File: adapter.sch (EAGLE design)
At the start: 14 parts

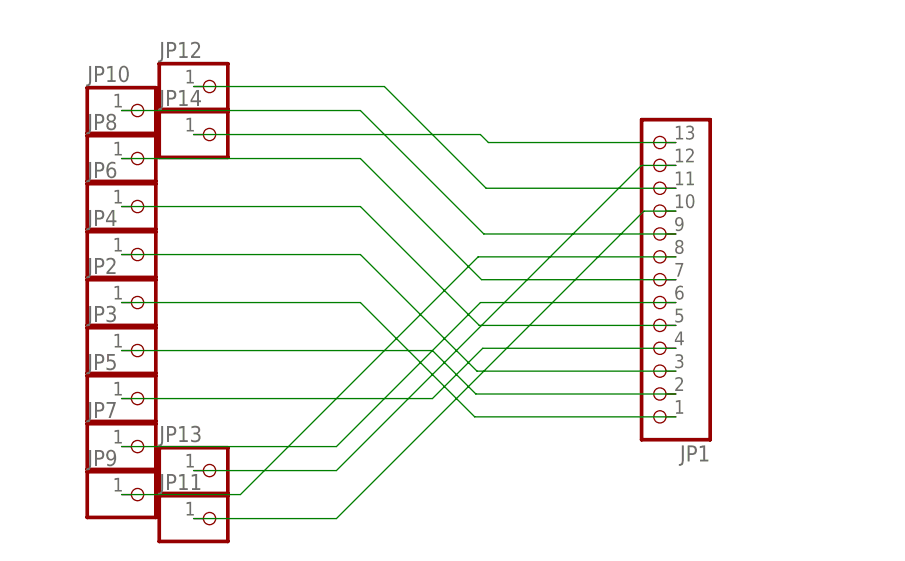
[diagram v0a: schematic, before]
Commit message: update adapter board for SMD
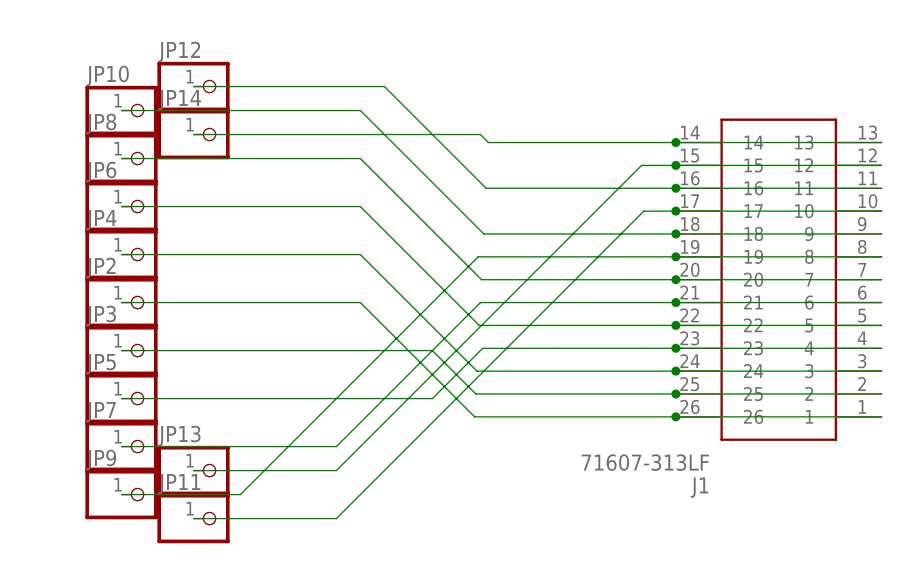
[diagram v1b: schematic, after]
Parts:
- removed JP1: (no value), pinhead:PINHD-1X13
- added J1: 71607-313LF, ltobms:71607-313LF
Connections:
- net N$1: now also J1.1, J1.26; no longer JP1.1
- net N$10: now also J1.10, J1.17; no longer JP1.10
- net N$11: now also J1.11, J1.16; no longer JP1.11
- net N$12: now also J1.12, J1.15; no longer JP1.12
- net N$13: now also J1.13, J1.14; no longer JP1.13
- net N$2: now also J1.2, J1.25; no longer JP1.2
- net N$3: now also J1.24, J1.3; no longer JP1.3
- net N$4: now also J1.23, J1.4; no longer JP1.4
- net N$5: now also J1.22, J1.5; no longer JP1.5
- net N$6: now also J1.21, J1.6; no longer JP1.6
- net N$7: now also J1.20, J1.7; no longer JP1.7
- net N$8: now also J1.19, J1.8; no longer JP1.8
- net N$9: now also J1.18, J1.9; no longer JP1.9

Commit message: add labels
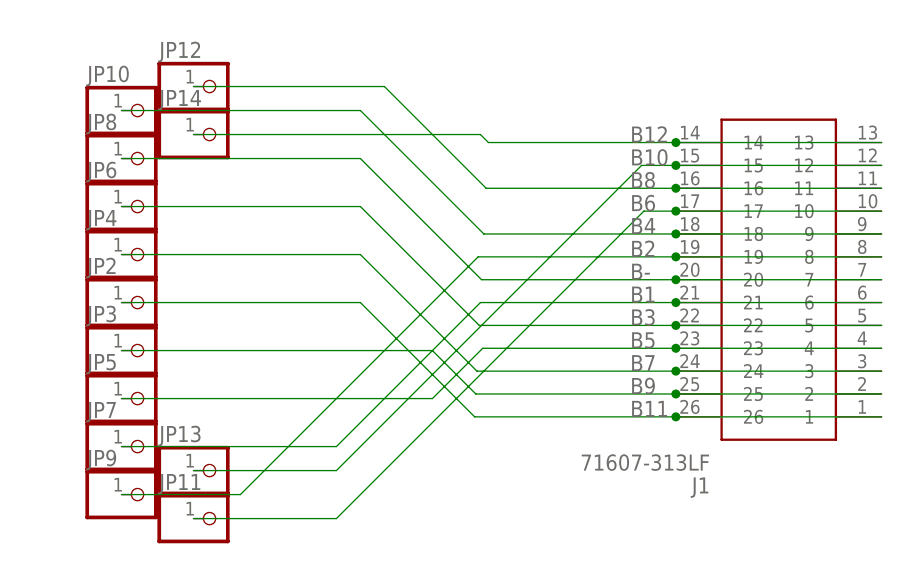
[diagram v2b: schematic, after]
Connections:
- net N$1 renamed B11
- net N$10 renamed B6
- net N$11 renamed B8
- net N$12 renamed B10
- net N$13 renamed B12
- net N$2 renamed B9
- net N$3 renamed B7
- net N$4 renamed B5
- net N$5 renamed B3
- net N$6 renamed B1
- net N$7 renamed B-
- net N$8 renamed B2
- net N$9 renamed B4
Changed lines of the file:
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@@
 </busses>
 <nets>
-<net name="N$1" class="1">
+<net name="B11" class="1">
 <segment>
 <wire x1="99.06" y1="40.64" x2="76.708" y2="40.64" width="0.1524" layer="91"/>
@@
 <wire x1="121.92" y1="40.64" x2="99.06" y2="40.64" width="0.1524" layer="91"/>
 <junction x="99.06" y="40.64"/>
+<label x="93.98" y="40.64" size="1.778" layer="95"/>
 </segment>
 </net>
-<net name="N$2" class="1">
+<net name="B9" class="1">
 <segment>
 <wire x1="99.06" y1="43.18" x2="76.835" y2="43.18" width="0.1524" layer="91"/>
@@
 <wire x1="121.92" y1="43.18" x2="99.06" y2="43.18" width="0.1524" layer="91"/>
 <junction x="99.06" y="43.18"/>
+<label x="93.98" y="43.18" size="1.778" layer="95"/>
 </segment>
 </net>
-<net name="N$3" class="1">
+<net name="B7" class="1">
 <segment>
 <wire x1="99.06" y1="45.72" x2="76.962" y2="45.72" width="0.1524" layer="91"/>
@@
 <wire x1="121.92" y1="45.72" x2="99.06" y2="45.72" width="0.1524" layer="91"/>
 <junction x="99.06" y="45.72"/>
+<label x="93.98" y="45.72" size="1.778" layer="95"/>
 </segment>
 </net>
-<net name="N$4" class="1">
+<net name="B5" class="1">
 <segment>
 <wire x1="99.06" y1="48.26" x2="77.597" y2="48.26" width="0.1524" layer="91"/>
@@
 <wire x1="121.92" y1="48.26" x2="99.06" y2="48.26" width="0.1524" layer="91"/>
 <junction x="99.06" y="48.26"/>
+<label x="93.98" y="48.26" size="1.778" layer="95"/>
 </segment>
 </net>
-<net name="N$5" class="1">
+<net name="B3" class="1">
 <segment>
 <wire x1="99.06" y1="50.8" x2="77.216" y2="50.8" width="0.1524" layer="91"/>
@@
 <wire x1="121.92" y1="50.8" x2="99.06" y2="50.8" width="0.1524" layer="91"/>
 <junction x="99.06" y="50.8"/>
+<label x="93.98" y="50.8" size="1.778" layer="95"/>
 </segment>
 </net>
-<net name="N$6" class="1">
+<net name="B1" class="1">
 <segment>
 <wire x1="99.06" y1="53.34" x2="77.343" y2="53.34" width="0.1524" layer="91"/>
@@
 <wire x1="121.92" y1="53.34" x2="99.06" y2="53.34" width="0.1524" layer="91"/>
 <junction x="99.06" y="53.34"/>
+<label x="93.98" y="53.34" size="1.778" layer="95"/>
 </segment>
 </net>
-<net name="N$7" class="1">
+<net name="B-" class="1">
 <segment>
 <wire x1="99.06" y1="55.88" x2="77.47" y2="55.88" width="0.1524" layer="91"/>
@@
 <wire x1="121.92" y1="55.88" x2="99.06" y2="55.88" width="0.1524" layer="91"/>
 <junction x="99.06" y="55.88"/>
+<label x="93.98" y="55.88" size="1.778" layer="95"/>
 </segment>
 </net>
-<net name="N$8" class="1">
+<net name="B2" class="1">
 <segment>
 <wire x1="99.06" y1="58.42" x2="77.089" y2="58.42" width="0.1524" layer="91"/>
@@
 <wire x1="121.92" y1="58.42" x2="99.06" y2="58.42" width="0.1524" layer="91"/>
 <junction x="99.06" y="58.42"/>
+<label x="93.98" y="58.42" size="1.778" layer="95"/>
 </segment>
 </net>
-<net name="N$9" class="1">
+<net name="B4" class="1">
 <segment>
 <wire x1="99.06" y1="60.96" x2="77.724" y2="60.96" width="0.1524" layer="91"/>
@@
 <wire x1="121.92" y1="60.96" x2="99.06" y2="60.96" width="0.1524" layer="91"/>
 <junction x="99.06" y="60.96"/>
+<label x="93.98" y="60.96" size="1.778" layer="95"/>
 </segment>
 </net>
-<net name="N$10" class="1">
+<net name="B6" class="1">
 <segment>
 <wire x1="99.06" y1="63.5" x2="95.504" y2="63.5" width="0.1524" layer="91"/>
@@
 <wire x1="121.92" y1="63.5" x2="99.06" y2="63.5" width="0.1524" layer="91"/>
 <junction x="99.06" y="63.5"/>
+<label x="93.98" y="63.5" size="1.778" layer="95"/>
 </segment>
 </net>
-<net name="N$11" class="1">
+<net name="B8" class="1">
 <segment>
 <wire x1="99.06" y1="66.04" x2="77.978" y2="66.04" width="0.1524" layer="91"/>
@@
 <wire x1="121.92" y1="66.04" x2="99.06" y2="66.04" width="0.1524" layer="91"/>
 <junction x="99.06" y="66.04"/>
+<label x="93.98" y="66.04" size="1.778" layer="95"/>
 </segment>
 </net>
-<net name="N$12" class="1">
+<net name="B10" class="1">
 <segment>
 <wire x1="99.06" y1="68.58" x2="95.25" y2="68.58" width="0.1524" layer="91"/>
@@
 <wire x1="121.92" y1="68.58" x2="99.06" y2="68.58" width="0.1524" layer="91"/>
 <junction x="99.06" y="68.58"/>
+<label x="93.98" y="68.58" size="1.778" layer="95"/>
 </segment>
 </net>
-<net name="N$13" class="1">
+<net name="B12" class="1">
 <segment>
 <wire x1="99.06" y1="71.12" x2="78.232" y2="71.12" width="0.1524" layer="91"/>
@@
 <wire x1="121.92" y1="71.12" x2="99.06" y2="71.12" width="0.1524" layer="91"/>
 <junction x="99.06" y="71.12"/>
+<label x="93.98" y="71.12" size="1.778" layer="95"/>
 </segment>
 </net>

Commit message: fix labels
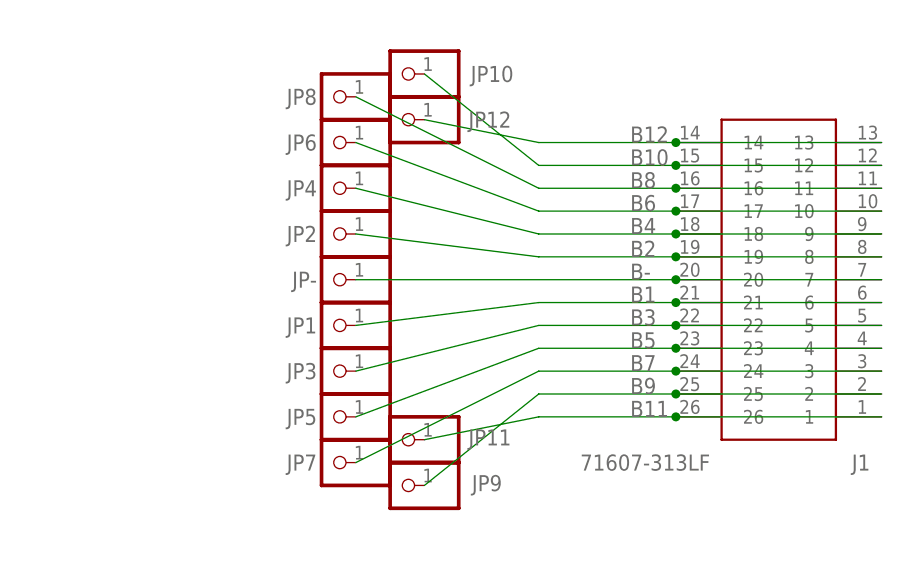
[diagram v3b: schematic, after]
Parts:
- removed JP13, JP14: (no value), pinhead:PINHD-1X1
- added JP-, JP1: (no value), ltobms:PINHD-1X1
- JP10, JP11, JP12, JP2, JP3, JP4, JP5, JP6, JP7, JP8, JP9: device pinhead:PINHD-1X1 -> ltobms:PINHD-1X1
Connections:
- net B-: now also JP-.1; no longer JP8.1
- net B1: now also JP1.1; no longer JP7.1
- net B10: now also JP10.1; no longer JP13.1
- net B11: now also JP11.1; no longer JP2.1
- net B12: now also JP12.1; no longer JP14.1
- net B2: now also JP2.1; no longer JP9.1
- net B3: now also JP3.1; no longer JP6.1
- net B4: now also JP4.1; no longer JP10.1
- net B6: now also JP6.1; no longer JP11.1
- net B7: now also JP7.1; no longer JP4.1
- net B8: now also JP8.1; no longer JP12.1
- net B9: now also JP9.1; no longer JP3.1
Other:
- moved on the sheet: JP10, JP11, JP12, JP2, JP3, JP4, JP5, JP6, JP7, JP8, JP9

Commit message: add samtec footprint for more compatibility
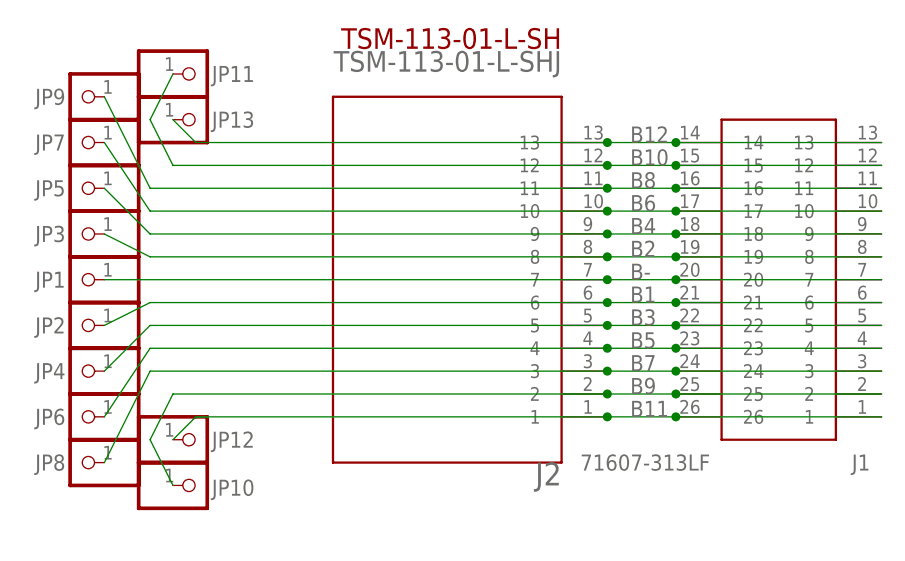
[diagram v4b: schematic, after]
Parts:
- removed JP-: (no value), ltobms:PINHD-1X1
- added J2: TSM-113-01-L-SHJ, ltobms:TSM-113-01-L-SHJ
- added JP13: (no value), ltobms:PINHD-1X1
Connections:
- net B-: now also J2.7, JP1.1; no longer JP-.1
- net B1: now also J2.6, JP2.1; no longer JP1.1
- net B10: now also J2.12, JP11.1; no longer JP10.1
- net B11: now also J2.1, JP12.1; no longer JP11.1
- net B12: now also J2.13, JP13.1; no longer JP12.1
- net B2: now also J2.8, JP3.1; no longer JP2.1
- net B3: now also J2.5, JP4.1; no longer JP3.1
- net B4: now also J2.9, JP5.1; no longer JP4.1
- net B5: now also J2.4, JP6.1; no longer JP5.1
- net B6: now also J2.10, JP7.1; no longer JP6.1
- net B7: now also J2.3, JP8.1; no longer JP7.1
- net B8: now also J2.11, JP9.1; no longer JP8.1
- net B9: now also J2.2, JP10.1; no longer JP9.1
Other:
- moved on the sheet: JP1, JP10, JP11, JP12, JP2, JP3, JP4, JP5, JP6, JP7, JP8, JP9
